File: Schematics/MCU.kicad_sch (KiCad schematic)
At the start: 45 parts, among them J7 Microsemi_FlashPro-JTAG-10, SW3 SW_Push, SW4 SW_Push, U1 STM32F405RGTx, U2 STM32F405RGTx, Y1 8mhz

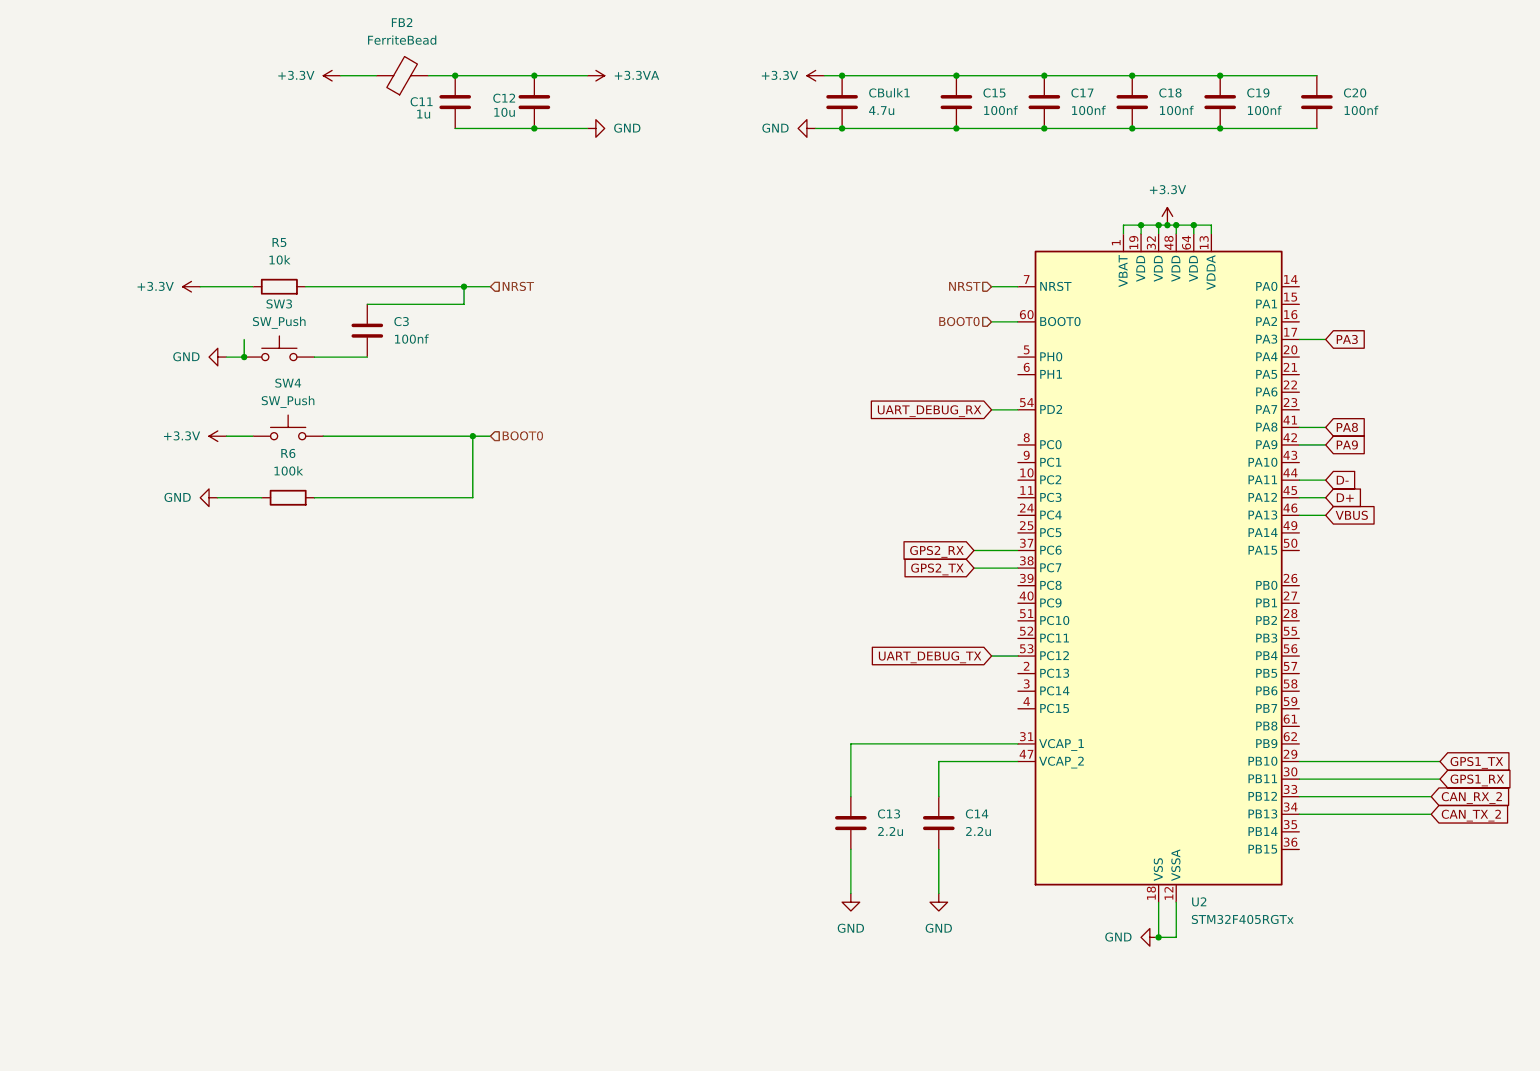
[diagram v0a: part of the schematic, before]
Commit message: Added SD SPI reader, Fixed file structure
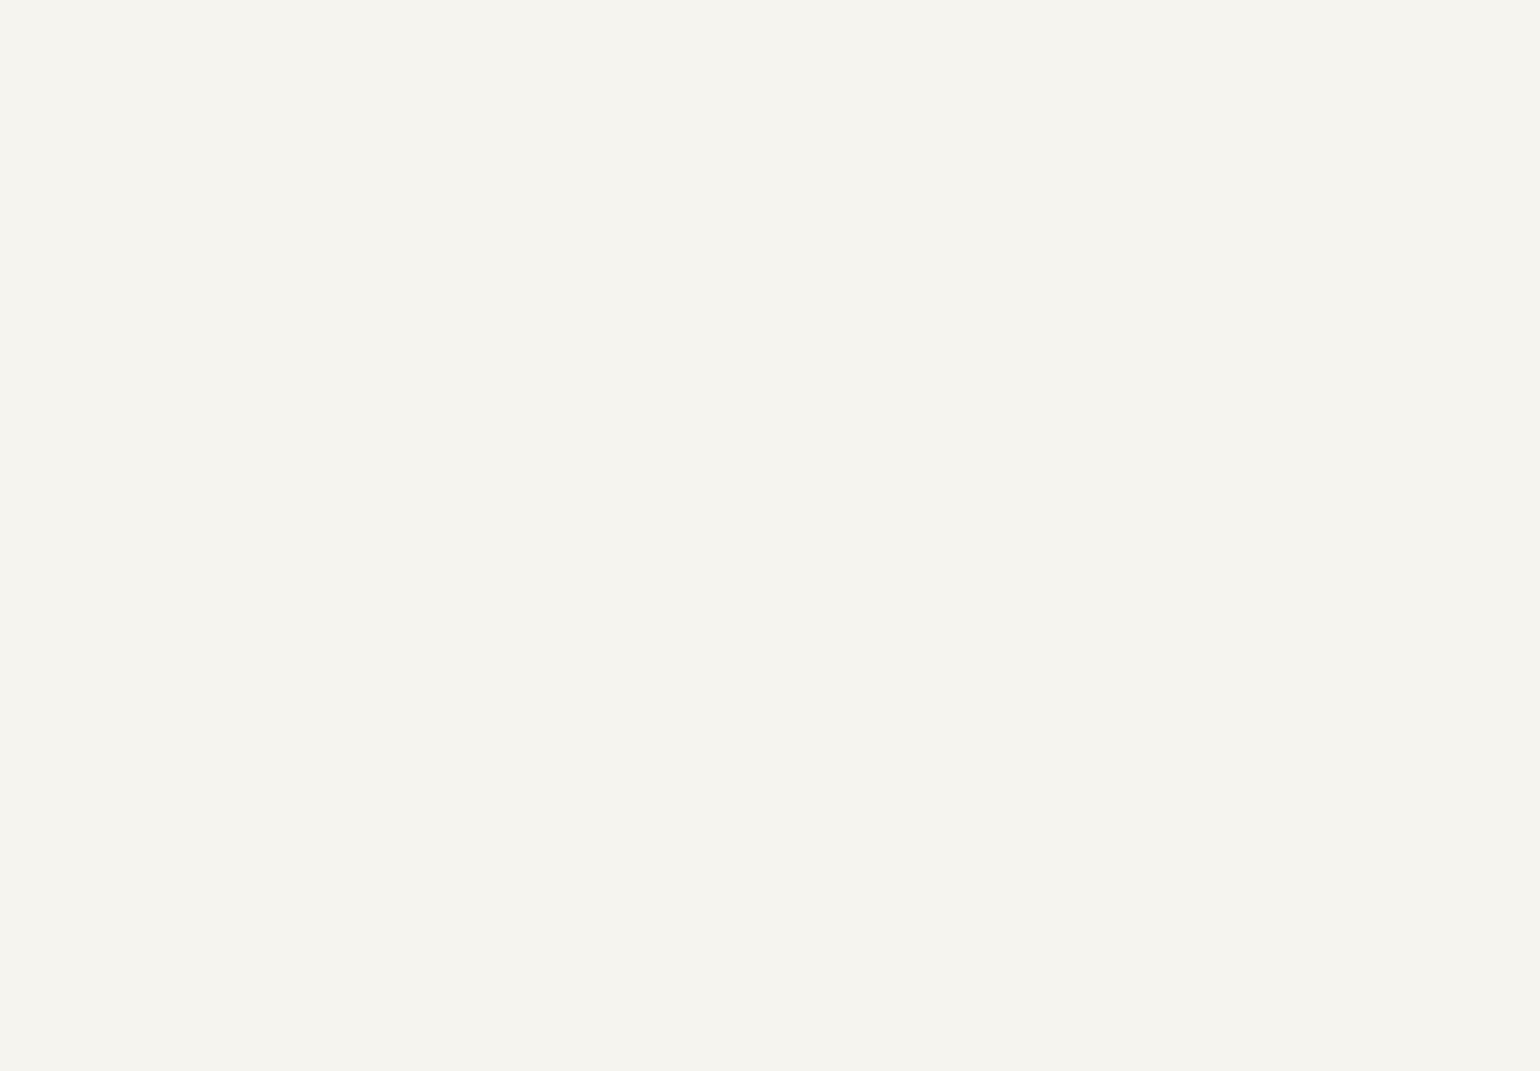
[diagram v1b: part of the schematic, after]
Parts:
- removed C11: 1u, Capacitor_SMD:C_0805_2012Metric_Pad1.18x1.45mm_HandSolder, symbol Device:C
- removed C12: 10u, Capacitor_SMD:C_0805_2012Metric_Pad1.18x1.45mm_HandSolder, symbol Device:C
- removed C13, C14: 2.2u, Capacitor_SMD:C_0805_2012Metric_Pad1.18x1.45mm_HandSolder, symbol Device:C
- removed C15, C17, C18, C19, C20, C3: 100nf, Capacitor_SMD:C_0805_2012Metric_Pad1.18x1.45mm_HandSolder, symbol Device:C
- removed CBulk1: 4.7u, Capacitor_SMD:C_0805_2012Metric_Pad1.18x1.45mm_HandSolder, symbol Device:C
- removed FB2: FerriteBead, Resistor_SMD:R_0805_2012Metric_Pad1.20x1.40mm_HandSolder, symbol Device:FerriteBead
- removed R5: 10k, Resistor_SMD:R_0805_2012Metric_Pad1.20x1.40mm_HandSolder, symbol Device:R
- removed R6: 100k, Resistor_SMD:R_0805_2012Metric_Pad1.20x1.40mm_HandSolder, symbol Device:R
- removed SW3, SW4: SW_Push, Library:SAMZO G4R0015010, symbol Switch:SW_Push
- removed U2: STM32F405RGTx, Package_QFP:LQFP-64_10x10mm_P0.5mm, symbol MCU_ST_STM32F4:STM32F405RGTx

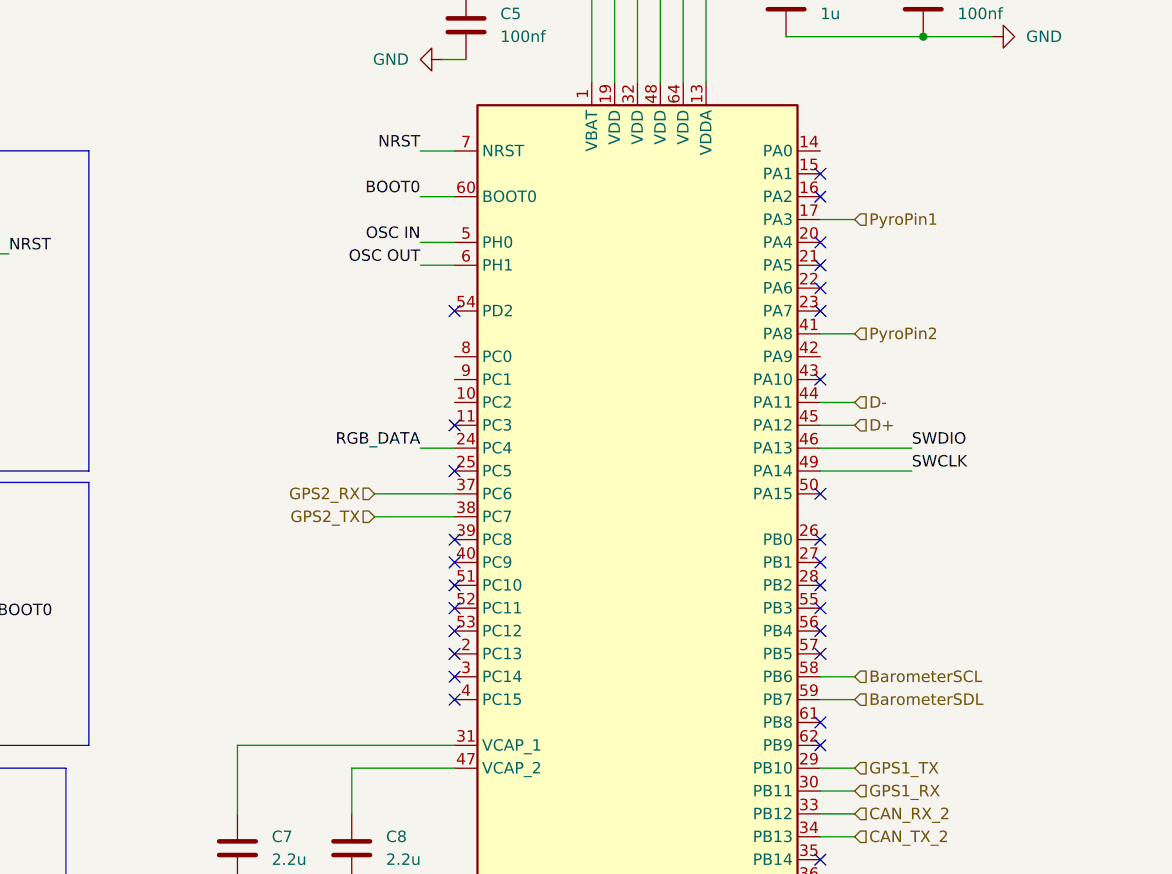
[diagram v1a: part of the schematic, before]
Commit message: finished sensor schematics, added datasheets organized files
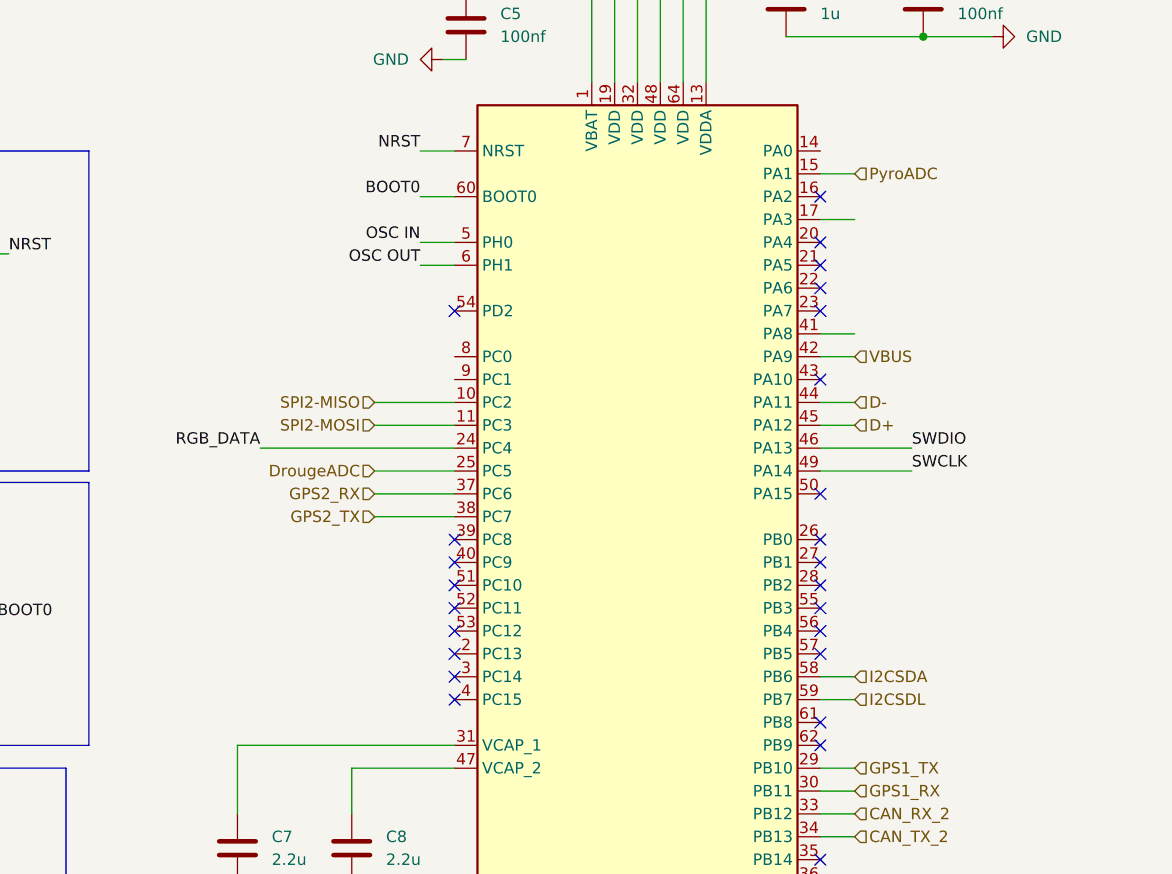
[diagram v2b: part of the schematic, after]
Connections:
- net SPI2-MISO: now reaches U1.10 (PC2)
- net SPI2-MOSI: now reaches U1.11 (PC3)
- net PyroADC: now reaches U1.15 (PA1)
- net DrougeADC: now reaches U1.25 (PC5)
- net VBUS: now reaches U1.42 (PA9)
- net BarometerSCL renamed I2CSDA
- net BarometerSDL renamed I2CSDL
- net PyroPin1: no longer names the net of U1.17 (PA3)
- net PyroPin2: no longer names the net of U1.41 (PA8)
- no-connect marks 34 -> 31
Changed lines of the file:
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@@
-	)
-	(no_connect
-		(at 120.65 107.95)
 	)
 	(no_connect
@@
 		(at 120.65 125.73)
 	)
-	(no_connect
-		(at 161.29 80.01)
-	)
-	(no_connect
-		(at 120.65 113.03)
-	)
 	(wire
 		(pts
@@
 	(wire
 		(pts
+			(xy 111.76 105.41) (xy 120.65 105.41)
+		)
+		(stroke
+			(width 0)
+			(type default)
+		)
+	)
+	(wire
+		(pts
 			(xy 143.51 36.83) (xy 143.51 69.85)
 		)
@@
 	(wire
 		(pts
+			(xy 111.76 107.95) (xy 120.65 107.95)
+		)
+		(stroke
+			(width 0)
+			(type default)
+		)
+	)
+	(wire
+		(pts
 			(xy 146.05 46.99) (xy 146.05 69.85)
 		)
@@
 	(wire
 		(pts
-			(xy 116.84 110.49) (xy 120.65 110.49)
+			(xy 99.06 110.49) (xy 120.65 110.49)
 		)
 		(stroke
@@
 	(wire
 		(pts
+			(xy 165.1 100.33) (xy 161.29 100.33)
+		)
+		(stroke
+			(width 0)
+			(type default)
+		)
+	)
+	(wire
+		(pts
 			(xy 96.52 143.51) (xy 96.52 151.13)
 		)
@@
 	(wire
 		(pts
+			(xy 165.1 80.01) (xy 161.29 80.01)
+		)
+		(stroke
+			(width 0)
+			(type default)
+		)
+	)
+	(wire
+		(pts
 			(xy 165.1 148.59) (xy 161.29 148.59)
 		)
@@
 		(pts
 			(xy 167.64 44.45) (xy 157.48 44.45)
+		)
+		(stroke
+			(width 0)
+			(type default)
+		)
+	)
+	(wire
+		(pts
+			(xy 111.76 113.03) (xy 120.65 113.03)
 		)
 		(stroke
@@
 	)
 	(label "RGB_DATA"
-		(at 116.84 110.49 180)
+		(at 99.06 110.49 180)
 		(effects
 			(font
@@
 		)
 	)
-	(hierarchical_label "PyroPin2"
-		(shape input)
-		(at 165.1 97.79 0)
+	(hierarchical_label "SPI2-MOSI"
+		(shape input)
+		(at 111.76 107.95 180)
+		(effects
+			(font
+				(size 1.27 1.27)
+			)
+			(justify right)
+		)
+	)
+	(hierarchical_label "D+"
+		(shape input)
+		(at 165.1 107.95 0)
 		(effects
 			(font
@@
 		)
 	)
-	(hierarchical_label "D+"
-		(shape input)
-		(at 165.1 107.95 0)
+	(hierarchical_label "GPS2_TX"
+		(shape input)
+		(at 111.76 118.11 180)
+		(effects
+			(font
+				(size 1.27 1.27)
+			)
+			(justify right)
+		)
+	)
+	(hierarchical_label "VBUS"
+		(shape input)
+		(at 165.1 100.33 0)
 		(effects
 			(font
@@
 		)
 	)
-	(hierarchical_label "GPS2_TX"
-		(shape input)
-		(at 111.76 118.11 180)
+	(hierarchical_label "SPI2-MISO"
+		(shape input)
+		(at 111.76 105.41 180)
 		(effects
 			(font
@@
 		)
 	)
-	(hierarchical_label "BarometerSDL"
+	(hierarchical_label "PyroADC"
+		(shape input)
+		(at 165.1 80.01 0)
+		(effects
+			(font
+				(size 1.27 1.27)
+			)
+			(justify left)
+		)
+	)
+	(hierarchical_label "I2CSDL"
 		(shape input)
 		(at 165.1 138.43 0)
@@
 		)
 	)
-	(hierarchical_label "PyroPin1"
-		(shape input)
-		(at 165.1 85.09 0)
+	(hierarchical_label "DrougeADC"
+		(shape input)
+		(at 111.76 113.03 180)
+		(effects
+			(font
+				(size 1.27 1.27)
+			)
+			(justify right)
+		)
+	)
+	(hierarchical_label "GPS1_TX"
+		(shape input)
+		(at 165.1 146.05 0)
 		(effects
 			(font
@@
 		)
 	)
-	(hierarchical_label "GPS1_TX"
-		(shape input)
-		(at 165.1 146.05 0)
+	(hierarchical_label "GPS1_RX"
+		(shape input)
+		(at 165.1 148.59 0)
 		(effects
 			(font
@@
 		)
 	)
-	(hierarchical_label "GPS1_RX"
-		(shape input)
-		(at 165.1 148.59 0)
-		(effects
-			(font
-				(size 1.27 1.27)
-			)
-			(justify left)
-		)
-	)
-	(hierarchical_label "BarometerSCL"
+	(hierarchical_label "I2CSDA"
 		(shape input)
 		(at 165.1 135.89 0)
